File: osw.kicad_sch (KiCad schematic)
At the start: 67 parts, among them J1 Conn_01x02, Q1 2N7002, SW1 SW_Push, SW2 SW_Push, SW4 SW_Push, SW5 SW_Push, U1 DS3231MZ, U10 XC6209, U11 MCP73831T-2ACI_OT, U13 XC6209, U2 BMA400, U3 PSRAM64H, U4 GC9A01_IPS_display, U5 USB-OTG, U6 CH340E, U7 ttgo-32-micro, U8 Quectel_L96, U9 TPS2115A

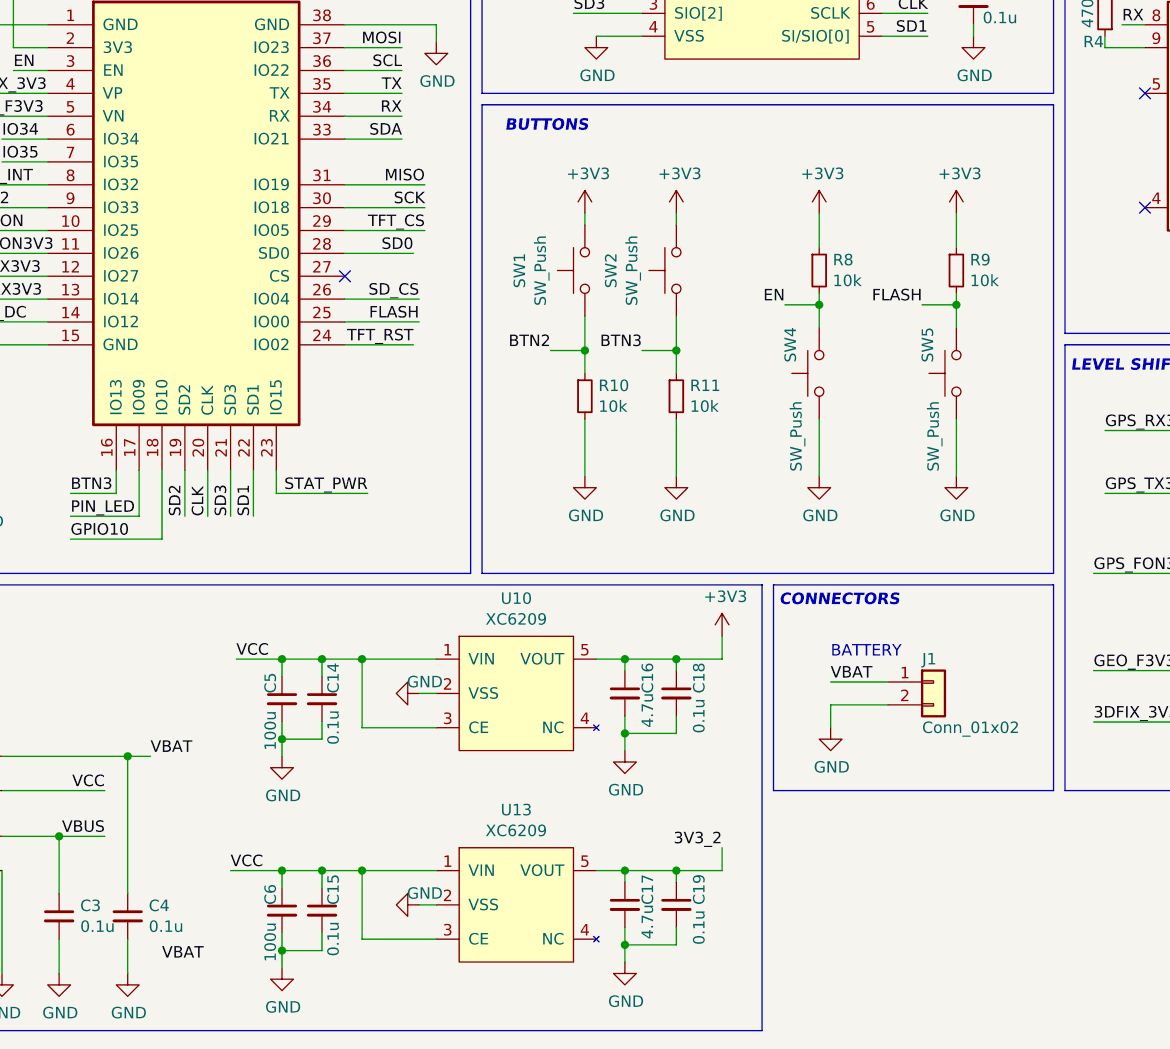
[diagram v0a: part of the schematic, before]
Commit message: Continuing to update symbols and models and moving all symbols to metric grids.
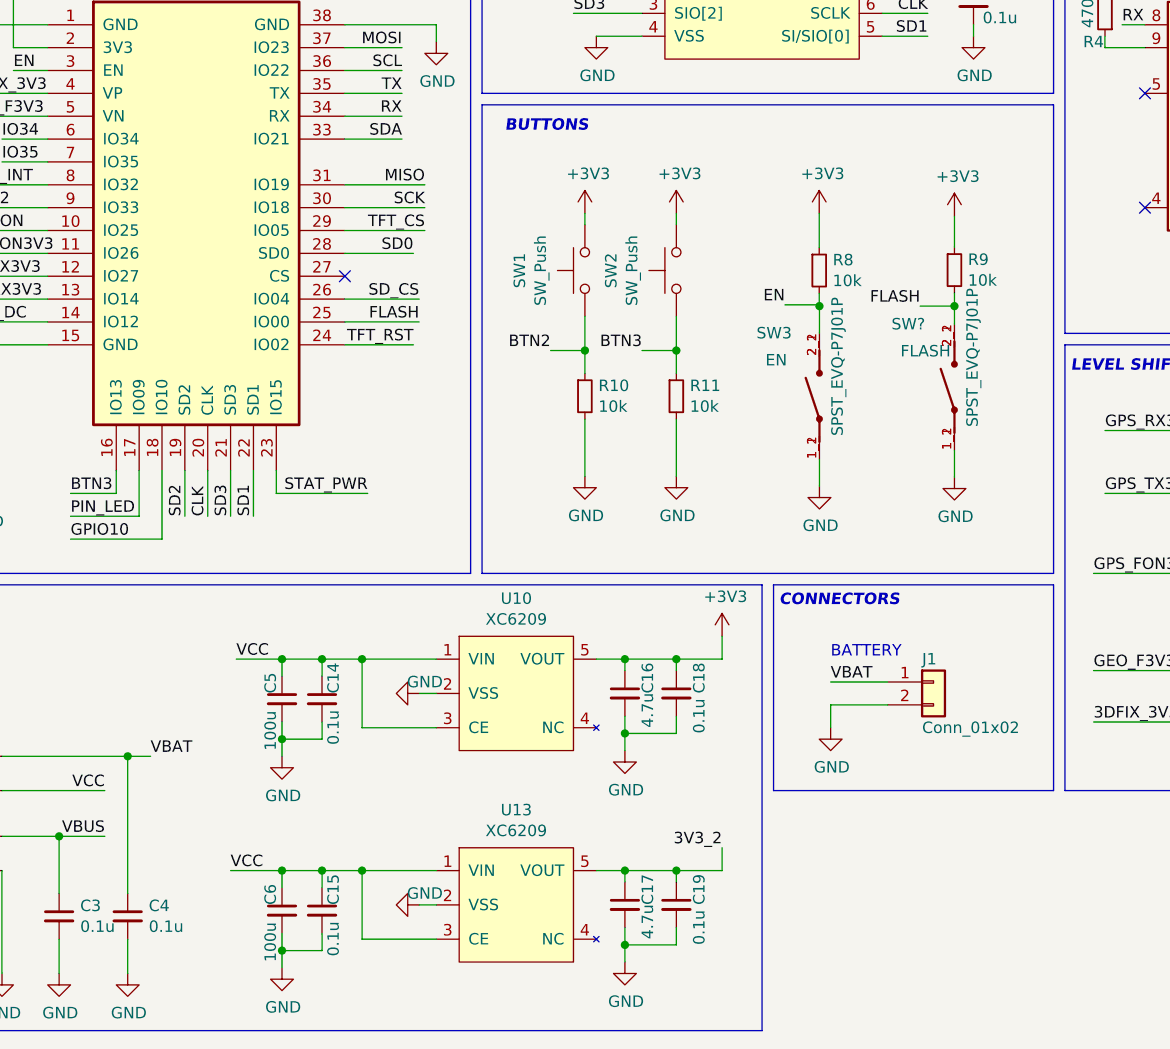
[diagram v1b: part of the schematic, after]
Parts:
- removed SW4, SW5: SW_Push, open-Smartwatch:button_side_smd, symbol Switch:SW_Push
- added SW3, SW?: SPST_EVQ-P7J01P, open-Smartwatch:SW_EVQ-P7J01P, symbol open-Smartwatch:SPST_EVQ-P7J01P
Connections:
- net FLASH: now also SW?.2_1, SW?.2_2
- net GND: now also SW3.1_1, SW3.1_2, SW?.1_1, SW?.1_2
- new net: SW3.2_1, SW3.2_2

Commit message: Updates to the board and schematic.
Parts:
- removed C12, C9: 0.1u, Capacitor_SMD:C_0603_1608Metric, symbol Device:C_Small
- removed R10, R11, R17, R21, R8, R9: 10k, Resistor_SMD:R_0603_1608Metric, symbol Device:R_Small
- removed R6, R7: 1k, Resistor_SMD:R_0603_1608Metric, symbol Device:R_Small
- removed SW1, SW2: SW_Push, open-Smartwatch:button_side_smd, symbol Switch:SW_Push
- removed U6: CH340E, open-Smartwatch:MSOP-10_3x3mm_P0.5mm, symbol open-Smartwatch:CH340E
- added C?: 1u, open-Smartwatch:C_0402_1005Metric_osw, symbol open-Smartwatch:cap0402_p1u10V
- added C?: cap0402_p1u10V, open-Smartwatch:C_0402_1005Metric_osw, symbol open-Smartwatch:cap0402_p1u10V
- added R10, R11, R8, R9, R? (x4): res0402_10k, open-Smartwatch:R_0402_1005Metric_osw, symbol open-Smartwatch:res0402_10k
- added SW1, SW2: SPST_EVQ-P7J01P, open-Smartwatch:SW_EVQ-P7J01P, symbol open-Smartwatch:SPST_EVQ-P7J01P
- added U?: FT234XD-R, open-Smartwatch:SON45P300X300X80-13N, symbol open-Smartwatch:FT234XD-R
- gave numbers to parts that had none: 1
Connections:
- net +3V3: now also R10.1, R11.1, R?.1, R?.1, SW1.2_1, SW1.2_2, SW2.2_1, SW2.2_2; no longer U3.8 (VCC)
- net BTN2: now also R8.1, SW1.1_1, SW1.1_2
- net BTN3: now also R9.1, SW2.1_1, SW2.1_2
- net B_MON: now also R?.1
- net CLK: no longer U3.6 (SCLK)
- net EN: now also SW3.2_1, SW3.2_2, R10.2
- net FLASH: now also R11.2
- net GND: now also R8.2, R9.2, R?.2; no longer U3.4 (VSS)
- net GPIO10: no longer U3.1 (CE#)
- net LEDK: no longer Q1.3 (D)
- net PIN_LED: now also R?.1
- net SCL: now also R?.2
- net SD0: no longer U3.2 (SO/SIO[1])
- net SD1: no longer U3.5 (SI/SIO[0])
- net SD2: no longer U3.7 (SIO[3])
- net SD3: no longer U3.3 (SIO[2])
- net SDA: now also R?.2
- net at Q1.1 (G), R22.2: now also R?.2
- new net: C?.1, U?.3 (3V3OUT), U?.4 (VCC), U?.9 (VCCIO)
- new net: C?.2, U?.5 (GND)
- no-connect marks 18 -> 15
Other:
- moved on the sheet: U3

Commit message: Adding a very small regulater for running everything.
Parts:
- removed C1, C2: 4.7uF, Capacitor_SMD:C_0603_1608Metric, symbol Device:C_Small
- removed C14, C15, C18, C19, C3, C4, C7: 0.1u, Capacitor_SMD:C_0603_1608Metric, symbol Device:C_Small
- removed C16, C17: 4.7u, Capacitor_SMD:C_0603_1608Metric, symbol Device:C_Small
- removed C5, C6: 100u, Capacitor_SMD:C_1206_3216Metric, symbol Device:C_Small
- removed R14: 510R, Resistor_SMD:R_0603_1608Metric, symbol Device:R_Small
- removed R19: 200k, Resistor_SMD:R_0603_1608Metric, symbol Device:R_Small
- removed R4: 470R, Resistor_SMD:R_0603_1608Metric, symbol Device:R_Small
- removed U10, U13: XC6209, Package_TO_SOT_SMD:SOT-23-5, symbol open-Smartwatch:XC6209
- removed U3: PSRAM64H, Package_SO:SOP-8_3.9x4.9mm_P1.27mm, symbol open-Smartwatch:PSRAM64H
- removed U5: USB-OTG, open-Smartwatch:USBmicro-B, symbol open-Smartwatch:USB-OTG
- removed U9: TPS2115A, open-Smartwatch:TSSOP-8_4.4x3mm_P0.65mm, symbol open-Smartwatch:TPS2115A_default
- removed XS1: SD_ebay-uSD-push_push_SMD, open-Smartwatch:Conn_uSDcard, symbol open-Smartwatch:SD_ebay-uSD-push_push_SMD
- added C? (x5): cap0402_p1u10V, open-Smartwatch:C_0402_1005Metric_osw, symbol open-Smartwatch:cap0402_p1u10V
- added C? (x4): cap0402_4p7u10V, open-Smartwatch:C_0402_1005Metric_osw, symbol open-Smartwatch:cap0402_4p7u10V
- added J?: microSD_MEM2067-02-180-00-A_REVB, open-Smartwatch:GCT_MEM2067-02-180-00-A_REVB, symbol open-Smartwatch:microSD_MEM2067-02-180-00-A_REVB
- added J?: usbc_USB4056-03-A, open-Smartwatch:GCT_USB4056-03-A_REVA, symbol open-Smartwatch:usbc_USB4056-03-A
- added U? (x2): MIC5504-3p3, open-Smartwatch:VREG_MIC5504-3.3YMT-TZ, symbol open-Smartwatch:MIC5504-3p3
- added U?: PSRAM64H, symbol open-Smartwatch:PSRAM64H
- added U?: TPS22933, open-Smartwatch:uqfn_1p5x1p5_8_tps22933, symbol open-Smartwatch:TPS22933
- C12, C9: renamed from C?; Capacitance (none) -> 0.1u
- U11: DigiKey_PN (none) -> MCP73831T-2ACI/OTCT-ND
- gave numbers to parts that had none: 5
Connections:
- net +3V3: now also C12.1, C9.1, U6.2 (~{RESET#}), U6.3 (3V3OUT), U6.9 (VCCIO), C?.1, C?.1, J?.4 (VDD), U?.1 (VOUT), U?.8 (VCC)
- net 3V3_2: now also C?.1, C?.1, U?.1 (VOUT)
- net CLK: now also U?.6 (SCLK)
- net D_N: now also U6.1 (USBDM), J?.A7 (DN1), J?.B7 (DN2)
- net D_P: now also U6.12 (USBDP), J?.A6 (DP1), J?.B6 (DP2)
- net GND: now also C12.2, C9.2, U6.13 (GND_PAD), U6.5 (GND), U6.6 (CBUS0), C?.1, C?.2, C?.2, C?.2, C?.2, C?.2, C?.2, C?.2, C?.2, J?.10 (SHIELD), J?.11 (SHIELD), J?.12 (SHIELD), J?.6 (VSS), J?.9 (SHIELD), J?.A1 (GND_A), J?.A12 (GND_A), J?.B1 (GND_B), J?.B12 (GND_B), J?.S1 (SHELL_GND), J?.S2 (SHELL_GND), J?.S3 (SHELL_GND), J?.S4 (SHELL_GND), U?.2 (GND), U?.2 (GND), U?.4 (GND), U?.4 (VSS), U?.5 (PAD), U?.5 (PAD); no longer R15.2
- net GPIO10: now also U?.1 (CE#)
- net MISO: now also J?.7 (MISO/DAT0)
- net MOSI: now also J?.3 (MOSI/CMD)
- net RX: now also U6.7 (TXD)
- net SCK: now also J?.5 (CLK)
- net SD0: now also U?.2 (SO/SIO[1])
- net SD1: now also U?.5 (SI/SIO[0])
- net SD2: now also U?.7 (SIO[3])
- net SD3: now also U?.3 (SIO[2])
- net SD_CS: now also J?.2 (CS/DAT3)
- net TX: now also U6.10 (RXD)
- net VBAT: now also C?.1, U?.1 (BAT)
- net VBUS: now also U6.4 (VCC), C?.2, J?.A4 (VBUS_A), J?.A9 (VBUS_A), J?.B4 (VBUS_B), J?.B9 (VBUS_B), U?.2 (USB)
- net VCC: now also C?.1, U?.4 (VIN), U?.4 (VIN), U?.5 (EN), U?.8 (LOUT)
- net at U11.1 (STAT): no longer D1.1 (K)
- net at U11.5 (PROG): no longer R15.1
- new net: C?.1, U?.6 (CAP)
- new net: C?.1, U?.7 (VOUT)
- no-connect marks 15 -> 13
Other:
- moved on the sheet: C12, C9, D1, R13, R15, R17, R21, U11

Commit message: Updates to the libs and the schematic.  Only need to update the battery charger a FET and a couple of resisters.  After that this should be good to go to layout.
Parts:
- removed C10, C11, C13, C8: 0.1u, Capacitor_SMD:C_0603_1608Metric, symbol Device:C_Small
- removed C20: 100p, Capacitor_SMD:C_0603_1608Metric, symbol Device:C_Small
- removed C21: 10p, Capacitor_SMD:C_0603_1608Metric, symbol Device:C_Small
- removed R12: 5.6k, Resistor_SMD:R_0603_1608Metric, symbol Device:R_Small
- removed R18: 2.2K, Resistor_SMD:R_0603_1608Metric, symbol Device:R_Small
- removed R2, R24, R25, R3: 1k, Resistor_SMD:R_0603_1608Metric, symbol Device:R_Small
- removed R20: 10k, Resistor_SMD:R_0603_1608Metric, symbol Device:R_Small
- removed R22: 1M, Resistor_SMD:R_0603_1608Metric, symbol Device:R_Small
- removed R23: 56k, Resistor_SMD:R_0603_1608Metric, symbol Device:R_Small
- removed R5: 0R, Resistor_SMD:R_0402_1005Metric, symbol Device:R_Small
- removed U1: DS3231MZ, Package_SO:SOIC-8_3.9x4.9mm_P1.27mm, symbol Timer_RTC:DS3231MZ
- removed U7: ttgo-32-micro, open-Smartwatch:ttgo-32-micro, symbol open-Smartwatch:ttgo-32-micro
- removed U8: Quectel_L96, open-Smartwatch:Quectel_L96, symbol open-Smartwatch:Quectel_L96
- added C? (x4): cap0402_p1u10V, open-Smartwatch:C_0402_1005Metric_osw, symbol open-Smartwatch:cap0402_p1u10V
- added C? (x2): cap0402_1p0u10V, open-Smartwatch:C_0402_1005Metric_osw, symbol open-Smartwatch:cap0402_1p0u10V
- added R? (x4): res0402_1k, open-Smartwatch:R_0402_1005Metric_osw, symbol open-Smartwatch:res0402_1k
- added R?: res0402_10k, open-Smartwatch:R_0402_1005Metric_osw, symbol open-Smartwatch:res0402_10k
- added R?: res0402_56k, open-Smartwatch:R_0402_1005Metric_osw, symbol open-Smartwatch:res0402_56k
- added R?: res0402_5p6k, open-Smartwatch:R_0402_1005Metric_osw, symbol open-Smartwatch:res0402_5p6k
- added U?: L96-M33, open-Smartwatch:XCVR_L96-M33, symbol open-Smartwatch:L96-M33
- added U?: PCF85063ATL/1,118, open-Smartwatch:10-DFN(2.6X2.6)_PCF85063A, symbol open-Smartwatch:PCF85063ATL/1,118
- added U?: BH1792GLC-E2, open-Smartwatch:XDCR_BH1792GLC-E2, symbol open-Smartwatch:BH1792GLC-E2
- added U?: ESP32-S3-WROOM, open-Smartwatch:XCVR_ESP32-S3-WROOM-1U, symbol open-Smartwatch:ESP32-S3-WROOM
- R10, R11, R17, R21, R6, R7, R8, R9: Resistance (none) -> 10k
- U11: Digi-Key_PN MCP73831T-2ACI/OTCT-ND -> (none)
- U?: renamed from U2; manf# (none) -> MPN
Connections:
- net +3V3: now also C?.1, C?.1, C?.1, C?.1, U?.1 (VCC), U?.10 (VDD), U?.2 (3V3); no longer U?.10 (CSB)
- net 3DFIX_2V8: now also R?.2, U?.2 (3D_FIX)
- net 3DFIX_3V3: now also R?.1
- net 3V3_2: now also R7.1, C?.1, C?.1, U?.8 (V_BCKP), U?.9 (VCC)
- net BTN3: now also U?.12 (IO8)
- net CLK: now also U?.20 (IO12)
- net EN: now also U?.3 (EN)
- net GEO_F2V8: now also R?.2, U?.24 (GEO_FENCE)
- net GEO_F3V3: now also R?.1
- net GND: now also C?.2, C?.2, C?.2, C?.2, C?.2, R?.2, R?.2, U?.1 (GND), U?.10 (GND), U?.11 (GND), U?.11 (VSS), U?.12 (GND), U?.13 (GND), U?.14 (GND), U?.15 (GND), U?.18 (GND), U?.19 (GND), U?.2 (GND), U?.21 (GND), U?.22 (GND), U?.27 (GND), U?.31 (GND), U?.38 (GND), U?.4 (GND), U?.40 (GND), U?.41 (GND_PAD), U?.5 (GND), U?.5 (VSS), U?.7 (TEST), U?.8 (NC); no longer U?.1 (SDO), U?.8 (GNDIO), U?.9 (GND)
- net GPIO10: now also U?.18 (IO10)
- net GPS_FON2V8: now also R?.1, R?.2, U?.28 (FORCE_ON)
- net GPS_FON3V3: now also R?.1
- net GPS_RX2V8: now also R?.1, R?.2, U?.26 (RXD1)
- net GPS_RX3V3: now also R?.1
- net GPS_TX2V8: now also R?.2, U?.25 (TXD1)
- net GPS_TX3V3: now also R?.1
- net LEDK: now also Q1.3 (D)
- net PIN_LED: now also Q1.1 (G), R7.2, U?.17 (IO09); no longer R7.1
- net RTC_INT: now also U?.4 (~{INT})
- net SCL: now also U?.10 (SCL), U?.6 (I2C_SCL), U?.7 (SCL)
- net SD1: now also U?.22 (IO14)
- net SD2: now also U?.19 (IO11)
- net SD3: now also U?.21 (IO13)
- net SDA: now also U?.3 (I2C_SDA), U?.6 (SDA), U?.9 (SDA)
- net STAT_PWR: now also U?.8 (IO15)
- net at U11.1 (STAT): now also D1.1 (K)
- net IO34: no longer names the net of U?.5 (INT1)
- net IO35: no longer names the net of U?.6 (INT2)
- new net: C?.2, U?.1 (SDO), U?.8 (GNDIO), U?.9 (GND)
- no-connect marks 13 -> 3
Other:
- note added: "I2C ADDR: 0x14 (7bit)"
- note added: "I2C ADDR: 0x20 (7bit)"
- note added: "I2C ADDR: 0x51 (7bit)"
- note added: "I2C ADDR: 0x5B (7bit)"
- note removed: "I2C addr 0x14"
- note removed: "I2C addr 0x68"
- moved on the sheet: C12, D1, R13, R16, R6, U?

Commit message: Updating the display connector footprint.
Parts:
- removed C22: 0.1u, Capacitor_SMD:C_0603_1608Metric, symbol Device:C_Small
- removed R1: 22, Resistor_SMD:R_0603_1608Metric, symbol Device:R_Small
- removed U4: GC9A01_IPS_display, open-Smartwatch:GC9A01_IPS_display, symbol open-Smartwatch:GC9A01_IPS_display_SPI
- added C?: cap0402_1p0u10V, open-Smartwatch:C_0402_1005Metric_osw, symbol open-Smartwatch:cap0402_1p0u10V
- added U?: GC9A01_IPS_display_SPI, open-Smartwatch:GC9A01_IPS_display, symbol open-Smartwatch:GC9A01_IPS_display_SPI
- gave numbers to parts that had none: 33
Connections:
- net 3V3_2: now also C?.1, U?.4 (VDD)
- net GND: now also C?.2, U?.1 (GND), U?.12 (GND), U?.5 (GND), U?.6 (GND)
- net LEDK: now also U?.2 (LEDK)
- net MOSI: now also U?.10 (SDI)
- net SCK: now also U?.9 (SCK)
- net TFT_CS: now also U?.8 (~{CS})
- net TFT_DC: now also U?.7 (D/C)
- net TFT_RST: now also U?.11 (~{RESET})

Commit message: Getting close to schemtatic done.  Still have RAM to figure out and need to finish backlight driver FET.  Otherwise schematiclly things are looking good.
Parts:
- removed D1: LED_Green, LED_SMD:LED_0805_2012Metric, symbol Device:LED_Small
- removed R13: 470R, Resistor_SMD:R_0603_1608Metric, symbol Device:R_Small
- removed R15: 5k, Resistor_SMD:R_0603_1608Metric, symbol Device:R_Small
- added D?: LED_redSMD, open-Smartwatch:Harvatek_LED_osw, symbol open-Smartwatch:LED_redSMD
- added R?: res0402_10k, open-Smartwatch:R_0402_1005Metric_osw, symbol open-Smartwatch:res0402_10k
- added R? (x2): res0402_470, open-Smartwatch:R_0402_1005Metric_osw, symbol open-Smartwatch:res0402_470
- added R?: res0402_0, open-Smartwatch:R_0402_1005Metric_osw, symbol open-Smartwatch:res0402_0
- U?: renamed from U11; Mouser_PN (none) -> 579-MCP73831T-2ACIOT; manf# (none) -> MCP73831T-2ACI/OT
- renumbered U12 to U?
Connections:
- net +3V3: no longer C12.1, U6.2 (~{RESET#}), U6.3 (3V3OUT), U6.9 (VCCIO)
- net 3V3_2: now also R?.1; no longer R7.1
- net BTN2: now also U3.24 (IO47)
- net BTN3: now also U3.25 (IO48); no longer U3.12 (IO8)
- net FLASH: now also U3.27 (IO0)
- net GND: now also R7.2, R?.2; no longer Q1.2 (S)
- net PIN_LED: now also R7.1; no longer R7.2
- net RX: now also U3.36 (RXD0)
- net SCL: now also U3.23 (IO21)
- net SD0: now also U3.12 (IO8)
- net SDA: now also U3.14 (IO20)
- net TFT_CS: now also U3.6 (IO6)
- net TX: now also U3.37 (TXD0)
- net VBUS: now also R?.2
- net VCC: no longer U7.4 (VIN)
- net at U?.1 (STAT): now also D?.1 (K)
- net at U?.5 (PROG): now also R?.1
- net VCC_SW: now reaches C7.1, U2.7 (VOUT)
- net VCC_SW: now also U7.4 (VIN)
- net at U1.16 (RF_OUT): now also R?.1
- net at U1.17 (RF_IN): now also R?.2
- net at U?.3 (LEDA): now also R?.2
- net v3p3USB: now reaches U3.16 (IO46)
- net v3p3USB: now also C12.1, U6.2 (~{RESET#}), U6.3 (3V3OUT), U6.9 (VCCIO)
- new net: D?.2 (A), R?.1
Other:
- moved on the sheet: C3, C4, R7, U?

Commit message: Finished schematic.  Ready to begin board layout.
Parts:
- removed Q1: 2N7002, Package_TO_SOT_SMD:SOT-23, symbol Transistor_FET:2N7002
- removed R16: 200k, Resistor_SMD:R_0603_1608Metric, symbol Device:R_Small
- removed U8: PSRAM64H, symbol open-Smartwatch:PSRAM64H
- added Q1: Q_NMOS_ToshibaSMD, open-Smartwatch:SOT95P247X115-3N, symbol open-Smartwatch:Q_NMOS_ToshibaSMD
- added R16, R20: res0402_10k, open-Smartwatch:R_0402_1005Metric_osw, symbol open-Smartwatch:res0402_10k
- added U12: esd_USB_IP4234CZ6, open-Smartwatch:SOT-457_ESD, symbol open-Smartwatch:esd_USB_IP4234CZ6
- added U8: 23K256-I/SN, open-Smartwatch:SOIC127P600X175-8N_microchipRAM, symbol open-Smartwatch:23K256-I/SN
- gave numbers to parts that had none: 9
- renumbered U5 to U?, U7 to U?
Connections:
- net CLK is gone; now on net MOSI: U3.20 (IO12)
- net SD0 is gone; now on net SD_CS: U3.12 (IO8)
- net SD2 is gone; now on net SCLK: U3.19 (IO11)
- net SD3 is gone; now on net MISO: U3.21 (IO13)
- net TFT_RST is gone; now on net ~{TFT_RST}: U11.11 (~{RESET})
- net +3V3: now also R16.1, U8.8 (VCC)
- net 3DFIX_3V3: now also U3.33 (IO40)
- net B_MON: now also U3.35 (IO42), R20.2
- net D_N: now also U12.3 (I/O2A); no longer J3.A7 (DN1), J3.B7 (DN2)
- net D_P: now also U12.1 (I/O1A); no longer J3.A6 (DP1), J3.B6 (DP2)
- net GEO_F3V3: now also U3.32 (IO39)
- net GND: now also Q1.2 (S), U12.2 (GND), U8.3 (NC), U8.4 (VSS)
- net GPS_FON3V3: now also U3.31 (IO38)
- net GPS_RX3V3: now also U3.30 (IO37)
- net GPS_TX3V3: now also U3.29 (IO36)
- net LEDK: now also Q1.3 (D)
- net MISO: now also U8.2 (SO)
- net MOSI: now also U8.5 (SI)
- net PIN_LED: now also U3.4 (IO4), Q1.1 (G); no longer U3.17 (IO09)
- net RTC_INT: now also U3.11 (IO18)
- net TFT_CS: now also U3.17 (IO09); no longer U3.6 (IO6)
- net VBAT: now also R20.1
- net VBUS: now also U12.5 (VB)
- net VCC: no longer U2.5 (EN)
- net VLoad_EN: now reaches U3.26 (IO45)
- net VLoad_EN: now also U2.5 (EN)
- net ~{TFT_RST}: now reaches U3.28 (IO35)
- net GPIO10 renamed RAM_CS
- net RAM_CS: now also U8.1 (~{CS})
- net SCK renamed SCLK
- net SCLK: now also U8.6 (SCK)
- net SD1 renamed RAM_HOLD
- net RAM_HOLD: now also R16.2, U8.7 (~{HOLD})
- new net D_N_ESD: J3.A7 (DN1), J3.B7 (DN2), U12.4 (I/O2B)
- new net D_P_ESD: J3.A6 (DP1), J3.B6 (DP2), U12.6 (I/O1B)
- no-connect marks 3 -> 5
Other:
- moved on the sheet: J3, R6

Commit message: Updating the docs for the schematic.  May need to swap out the ESP chip as it is quite wide for the board layout....
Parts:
- gave numbers to parts that had none: 2
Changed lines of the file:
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@@
   (symbol (lib_id "open-Smartwatch:MIC5504-3p3") (at 149 226 0) (unit 1)
     (in_bom yes) (on_board yes) (fields_autoplaced)
-    (property "Reference" "U?" (id 0) (at 149 214.63 0))
+    (property "Reference" "U5" (id 0) (at 149 214.63 0))
     (property "Value" "MIC5504-3p3" (id 1) (at 149 217.17 0))
     (property "Footprint" "open-Smartwatch:VREG_MIC5504-3.3YMT-TZ" (id 2) (at 150.27 239.97 0)
@@
   (symbol (lib_id "open-Smartwatch:MIC5504-3p3") (at 149 251 0) (unit 1)
     (in_bom yes) (on_board yes) (fields_autoplaced)
-    (property "Reference" "U?" (id 0) (at 149 240.03 0))
+    (property "Reference" "U7" (id 0) (at 149 240.03 0))
     (property "Value" "MIC5504-3p3" (id 1) (at 149 242.57 0))
     (property "Footprint" "open-Smartwatch:VREG_MIC5504-3.3YMT-TZ" (id 2) (at 150.27 264.97 0)
@@
       (reference "U4") (unit 1) (value "MCP73831T-2ACI_OT") (footprint "open-Smartwatch:SOT-23-5")
     )
+    (path "/1fb0b406-fdc4-42ea-89a7-3c61b077c77d"
+      (reference "U5") (unit 1) (value "MIC5504-3p3") (footprint "open-Smartwatch:VREG_MIC5504-3.3YMT-TZ")
+    )
     (path "/28c663a6-5e13-4b51-b6ba-0db50d813c1a"
       (reference "U6") (unit 1) (value "FT234XD-R") (footprint "open-Smartwatch:SON45P300X300X80-13N")
     )
+    (path "/6c5d8100-3868-4e3a-9883-2e3cea3cc795"
+      (reference "U7") (unit 1) (value "MIC5504-3p3") (footprint "open-Smartwatch:VREG_MIC5504-3.3YMT-TZ")
+    )
     (path "/a8f95da4-83d8-4dc7-a5bb-ed9669c2d19a"
       (reference "U8") (unit 1) (value "23K256-I/SN") (footprint "open-Smartwatch:SOIC127P600X175-8N_microchipRAM")
@@
       (reference "U13") (unit 1) (value "BH1792GLC-E2") (footprint "open-Smartwatch:XDCR_BH1792GLC-E2")
     )
-    (path "/1fb0b406-fdc4-42ea-89a7-3c61b077c77d"
-      (reference "U?") (unit 1) (value "MIC5504-3p3") (footprint "open-Smartwatch:VREG_MIC5504-3.3YMT-TZ")
-    )
-    (path "/6c5d8100-3868-4e3a-9883-2e3cea3cc795"
-      (reference "U?") (unit 1) (value "MIC5504-3p3") (footprint "open-Smartwatch:VREG_MIC5504-3.3YMT-TZ")
-    )
-  )
+  )
